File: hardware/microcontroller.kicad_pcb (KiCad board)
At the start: 2 copper layers, 50.8 x 78.7 mm, 49 parts, among them J5 1x2 jumper right-angle, J6 Conn_02x03_Odd_Even, J7 1x2 jumper right-angle, U1 74LVC2G125, U12 74AHC373, U13 74AHC74, U14 74AHC373, U15 74LVC138A, U17 74LVC138A, U18 74LVC2G125, U2 74AHC04, U3 74LV161A, U4 74LV161A, U5 74LV161A, U6 74LV161A, U7 74LV161A, U8 74LV164A, U9 74LV164A

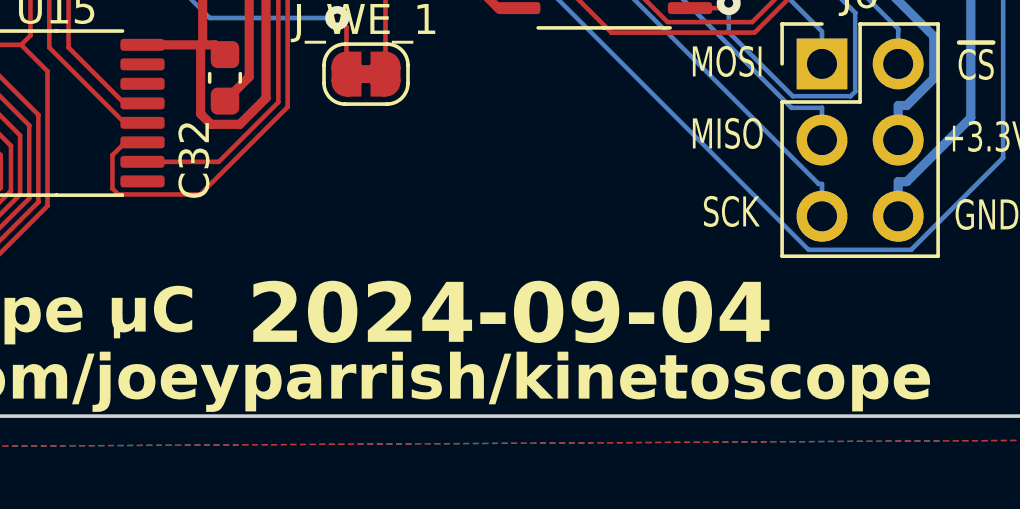
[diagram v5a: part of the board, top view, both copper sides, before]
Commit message: Replace 8-bit buffers with cheaper version
Replace SN74LVC8T245DBR (8-bit buffers) with SN74LVC8T245PWR.  The old
version was SSOP, and the new version is a TSSOP size, but they are
otherwise the same.

This is estimated to reduce the price of a complete unit by over $11,
or about 16.5%.
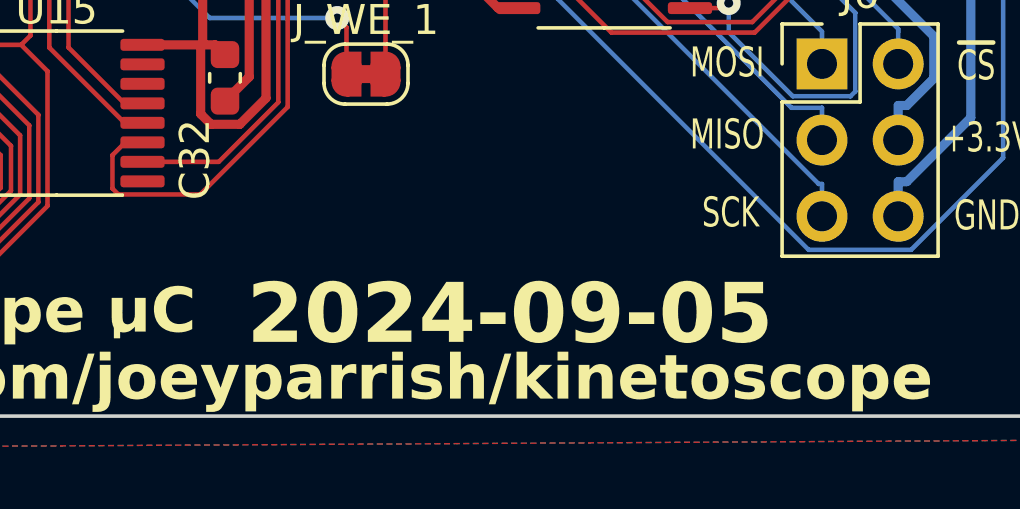
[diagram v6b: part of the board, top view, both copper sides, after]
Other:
- board text added: "2024-09-05"
- board text removed: "2024-09-04"
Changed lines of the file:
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@@
 		)
 	)
-	(gr_text "2024-09-04"
+	(gr_text "2024-09-05"
 		(at 51.64 94.64 0)
 		(layer "F.SilkS")
@@
 			)
 		)
-		(render_cache "2024-09-04" 0
+		(render_cache "2024-09-05" 0
 			(polygon
 				(pts
@@
 			(polygon
 				(pts
-					(xy 59.757655 94.56337) (xy 59.926671 94.56337) (xy 59.926671 94.807613) (xy 59.757655 94.807613)
-					(xy 59.757655 95.47) (xy 59.490453 95.47) (xy 59.490453 94.807613) (xy 58.742093 94.807613) (xy 58.489984 94.437341)
-					(xy 58.775799 94.437341) (xy 58.863238 94.56337) (xy 59.490453 94.56337) (xy 59.490453 93.703147)
-					(xy 58.775799 94.437341) (xy 58.489984 94.437341) (xy 58.46903 94.406566) (xy 59.369309 93.469162)
-					(xy 59.757655 93.469162)
+					(xy 58.553538 93.469162) (xy 59.783056 93.469162) (xy 59.783056 93.713405) (xy 58.817809 93.713405)
+					(xy 58.817809 94.042156) (xy 58.831975 94.069023) (xy 59.518785 94.069023) (xy 59.842163 94.548227)
+					(xy 59.842163 95.20866) (xy 59.594501 95.47) (xy 58.553538 95.47) (xy 58.553538 95.225757) (xy 59.48508 95.225757)
+					(xy 59.574961 95.131479) (xy 59.574961 94.584863) (xy 59.391779 94.313265) (xy 58.702526 94.313265)
+					(xy 58.553538 94.093935)
 				)
 			)

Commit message: Be consistent with SRAM bank numbering (0-1, not 1-2)
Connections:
- J2 pad 3: /SRAM_DIS_1 -> /SRAM_DIS_0
- J2 pad 4: /SRAM_DIS_2 -> /SRAM_DIS_1
- J3 pad 16: /SRAM_DIS_1 -> /SRAM_DIS_0
- J3 pad 17: /SRAM_DIS_2 -> /SRAM_DIS_1
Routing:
- net /SRAM_DIS_2: track 59.8 -> 0.00 mm
- net /SRAM_DIS_0: track 0.00 -> 50.1 mm
- net /SRAM_DIS_1: track 50.1 -> 59.8 mm
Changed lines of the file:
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@@
 	(net 25 "/kinetoscope-header-internal/SEGA_A11")
 	(net 26 "/kinetoscope-header-internal/SEGA_A17")
-	(net 27 "/SRAM_DIS_1")
-	(net 28 "/SRAM_DIS_2")
+	(net 27 "/SRAM_DIS_0")
+	(net 28 "/SRAM_DIS_1")
 	(net 29 "/kinetoscope-header-internal/SEGA_A22")
 	(net 30 "/kinetoscope-header-internal/SEGA_D12")
@@
 			(layers "*.Cu" "*.Mask")
 			(remove_unused_layers no)
-			(net 27 "/SRAM_DIS_1")
-			(pinfunction "SRAM_DIS_1")
+			(net 27 "/SRAM_DIS_0")
+			(pinfunction "SRAM_DIS_0")
 			(pintype "passive")
 		)
@@
 			(layers "*.Cu" "*.Mask")
 			(remove_unused_layers no)
-			(net 28 "/SRAM_DIS_2")
-			(pinfunction "SRAM_DIS_2")
+			(net 28 "/SRAM_DIS_1")
+			(pinfunction "SRAM_DIS_1")
 			(pintype "passive")
 		)
@@
 			(layers "*.Cu" "*.Mask")
 			(remove_unused_layers no)
-			(net 27 "/SRAM_DIS_1")
+			(net 27 "/SRAM_DIS_0")
 			(pinfunction "GP12")
 			(pintype "passive")
@@
 			(layers "*.Cu" "*.Mask")
 			(remove_unused_layers no)
-			(net 28 "/SRAM_DIS_2")
+			(net 28 "/SRAM_DIS_1")
 			(pinfunction "GP13")
 			(pintype "passive")
